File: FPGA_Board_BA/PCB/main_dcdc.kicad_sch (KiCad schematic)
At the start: 29 parts, among them Q2 IPT017N12NM6, Q3 IPT017N12NM6, Q4 IPT017N12NM6, Q5 IPT017N12NM6, U7 LM5143

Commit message: 22.11
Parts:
- renumbered D1 to D5, D2 to D6, D3 to D7, Q2 to Q1, Q3 to Q2, Q4 to Q3, Q5 to Q4, R8 to R1, R9 to R2, R10 to R3, R11 to R4, R12 to R5, R13 to R6, R14 to R7, U7 to U3
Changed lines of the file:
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@@
 		(on_board yes)
 		(dnp no)
-		(property "Reference" "#PWR022"
+		(property "Reference" "#PWR027"
 			(at 121.92 153.67 0)
 			(effects
@@
 			(project "FPGA_Board_BA"
 				(path "/fd7503bc-e7fc-4766-b224-3d1c3d7de5ff/c363a192-a091-4a49-a77c-8a6e46625814"
-					(reference "#PWR022")
+					(reference "#PWR027")
 					(unit 1)
 				)
@@
 		(on_board yes)
 		(dnp no)
-		(property "Reference" "#PWR023"
+		(property "Reference" "#PWR028"
 			(at 146.05 158.75 0)
 			(effects
@@
 			(project "FPGA_Board_BA"
 				(path "/fd7503bc-e7fc-4766-b224-3d1c3d7de5ff/c363a192-a091-4a49-a77c-8a6e46625814"
-					(reference "#PWR023")
+					(reference "#PWR028")
 					(unit 1)
 				)
@@
 		(dnp no)
 		(fields_autoplaced yes)
-		(property "Reference" "R10"
+		(property "Reference" "R3"
 			(at 101.6 52.07 90)
 			(effects
@@
 			(project ""
 				(path "/fd7503bc-e7fc-4766-b224-3d1c3d7de5ff/c363a192-a091-4a49-a77c-8a6e46625814"
-					(reference "R10")
+					(reference "R3")
 					(unit 1)
 				)
@@
 		(dnp no)
 		(fields_autoplaced yes)
-		(property "Reference" "D1"
+		(property "Reference" "D5"
 			(at 119.38 40.9574 90)
 			(effects
@@
 			(project ""
 				(path "/fd7503bc-e7fc-4766-b224-3d1c3d7de5ff/c363a192-a091-4a49-a77c-8a6e46625814"
-					(reference "D1")
+					(reference "D5")
 					(unit 1)
 				)
@@
 		(on_board yes)
 		(dnp no)
-		(property "Reference" "#PWR017"
+		(property "Reference" "#PWR022"
 			(at 62.23 44.45 0)
 			(effects
@@
 			(project "FPGA_Board_BA"
 				(path "/fd7503bc-e7fc-4766-b224-3d1c3d7de5ff/c363a192-a091-4a49-a77c-8a6e46625814"
-					(reference "#PWR017")
+					(reference "#PWR022")
 					(unit 1)
 				)
@@
 		(dnp no)
 		(fields_autoplaced yes)
-		(property "Reference" "D2"
+		(property "Reference" "D6"
 			(at 177.8 44.7674 90)
 			(effects
@@
 			(project ""
 				(path "/fd7503bc-e7fc-4766-b224-3d1c3d7de5ff/c363a192-a091-4a49-a77c-8a6e46625814"
-					(reference "D2")
+					(reference "D6")
 					(unit 1)
 				)
@@
 		(dnp no)
 		(fields_autoplaced yes)
-		(property "Reference" "R14"
+		(property "Reference" "R7"
 			(at 262.89 113.0299 0)
 			(effects
@@
 			(project ""
 				(path "/fd7503bc-e7fc-4766-b224-3d1c3d7de5ff/c363a192-a091-4a49-a77c-8a6e46625814"
-					(reference "R14")
+					(reference "R7")
 					(unit 1)
 				)
@@
 		(on_board yes)
 		(dnp no)
-		(property "Reference" "#PWR025"
+		(property "Reference" "#PWR030"
 			(at 163.83 55.88 0)
 			(effects
@@
 			(project "FPGA_Board_BA"
 				(path "/fd7503bc-e7fc-4766-b224-3d1c3d7de5ff/c363a192-a091-4a49-a77c-8a6e46625814"
-					(reference "#PWR025")
+					(reference "#PWR030")
 					(unit 1)
 				)
@@
 		(dnp no)
 		(fields_autoplaced yes)
-		(property "Reference" "Q5"
+		(property "Reference" "Q4"
 			(at 227.33 87.6299 0)
 			(effects
@@
 			(project "FPGA_Board_BA"
 				(path "/fd7503bc-e7fc-4766-b224-3d1c3d7de5ff/c363a192-a091-4a49-a77c-8a6e46625814"
-					(reference "Q5")
+					(reference "Q4")
 					(unit 1)
 				)
@@
 		(dnp no)
 		(fields_autoplaced yes)
-		(property "Reference" "R13"
+		(property "Reference" "R6"
 			(at 251.46 68.58 90)
 			(effects
@@
 			(project "FPGA_Board_BA"
 				(path "/fd7503bc-e7fc-4766-b224-3d1c3d7de5ff/c363a192-a091-4a49-a77c-8a6e46625814"
-					(reference "R13")
+					(reference "R6")
 					(unit 1)
 				)
@@
 		(dnp no)
 		(fields_autoplaced yes)
-		(property "Reference" "D3"
+		(property "Reference" "D7"
 			(at 264.16 126.0474 90)
 			(effects
@@
 			(project ""
 				(path "/fd7503bc-e7fc-4766-b224-3d1c3d7de5ff/c363a192-a091-4a49-a77c-8a6e46625814"
-					(reference "D3")
+					(reference "D7")
 					(unit 1)
 				)
@@
 		(on_board yes)
 		(dnp no)
-		(property "Reference" "Q2"
+		(property "Reference" "Q1"
 			(at 76.2 57.1499 0)
 			(effects
@@
 			(project ""
 				(path "/fd7503bc-e7fc-4766-b224-3d1c3d7de5ff/c363a192-a091-4a49-a77c-8a6e46625814"
-					(reference "Q2")
+					(reference "Q1")
 					(unit 1)
 				)
@@
 		(on_board yes)
 		(dnp no)
-		(property "Reference" "#PWR027"
+		(property "Reference" "#PWR032"
 			(at 223.52 104.14 0)
 			(effects
@@
 			(project "FPGA_Board_BA"
 				(path "/fd7503bc-e7fc-4766-b224-3d1c3d7de5ff/c363a192-a091-4a49-a77c-8a6e46625814"
-					(reference "#PWR027")
+					(reference "#PWR032")
 					(unit 1)
 				)
@@
 		(dnp no)
 		(fields_autoplaced yes)
-		(property "Reference" "R11"
+		(property "Reference" "R4"
 			(at 113.03 92.71 90)
 			(effects
@@
 			(project ""
 				(path "/fd7503bc-e7fc-4766-b224-3d1c3d7de5ff/c363a192-a091-4a49-a77c-8a6e46625814"
-					(reference "R11")
+					(reference "R4")
 					(unit 1)
 				)
@@
 		(dnp no)
 		(fields_autoplaced yes)
-		(property "Reference" "R12"
+		(property "Reference" "R5"
 			(at 201.93 55.88 90)
 			(effects
@@
 			(project "FPGA_Board_BA"
 				(path "/fd7503bc-e7fc-4766-b224-3d1c3d7de5ff/c363a192-a091-4a49-a77c-8a6e46625814"
-					(reference "R12")
+					(reference "R5")
 					(unit 1)
 				)
@@
 		(on_board yes)
 		(dnp no)
-		(property "Reference" "#PWR020"
+		(property "Reference" "#PWR025"
 			(at 99.06 139.7 0)
 			(effects
@@
 			(project "FPGA_Board_BA"
 				(path "/fd7503bc-e7fc-4766-b224-3d1c3d7de5ff/c363a192-a091-4a49-a77c-8a6e46625814"
-					(reference "#PWR020")
+					(reference "#PWR025")
 					(unit 1)
 				)
@@
 		(dnp no)
 		(fields_autoplaced yes)
-		(property "Reference" "Q4"
+		(property "Reference" "Q3"
 			(at 227.33 60.9599 0)
 			(effects
@@
 			(project "FPGA_Board_BA"
 				(path "/fd7503bc-e7fc-4766-b224-3d1c3d7de5ff/c363a192-a091-4a49-a77c-8a6e46625814"
-					(reference "Q4")
+					(reference "Q3")
 					(unit 1)
 				)
@@
 		(dnp no)
 		(fields_autoplaced yes)
-		(property "Reference" "#PWR029"
+		(property "Reference" "#PWR034"
 			(at 260.35 67.31 0)
 			(effects
@@
 			(project ""
 				(path "/fd7503bc-e7fc-4766-b224-3d1c3d7de5ff/c363a192-a091-4a49-a77c-8a6e46625814"
-					(reference "#PWR029")
+					(reference "#PWR034")
 					(unit 1)
 				)
@@
 		(on_board yes)
 		(dnp no)
-		(property "Reference" "R9"
+		(property "Reference" "R2"
 			(at 89.916 114.808 90)
 			(effects
@@
 			(project ""
 				(path "/fd7503bc-e7fc-4766-b224-3d1c3d7de5ff/c363a192-a091-4a49-a77c-8a6e46625814"
-					(reference "R9")
+					(reference "R2")
 					(unit 1)
 				)
@@
 		(on_board yes)
 		(dnp no)
-		(property "Reference" "#PWR019"
+		(property "Reference" "#PWR024"
 			(at 80.01 104.14 0)
 			(effects
@@
 			(project ""
 				(path "/fd7503bc-e7fc-4766-b224-3d1c3d7de5ff/c363a192-a091-4a49-a77c-8a6e46625814"
-					(reference "#PWR019")
+					(reference "#PWR024")
 					(unit 1)
 				)
@@
 		(dnp no)
 		(fields_autoplaced yes)
-		(property "Reference" "R8"
+		(property "Reference" "R1"
 			(at 43.18 64.77 90)
 			(effects
@@
 			(project ""
 				(path "/fd7503bc-e7fc-4766-b224-3d1c3d7de5ff/c363a192-a091-4a49-a77c-8a6e46625814"
-					(reference "R8")
+					(reference "R1")
 					(unit 1)
 				)
@@
 		(on_board yes)
 		(dnp no)
-		(property "Reference" "#PWR018"
+		(property "Reference" "#PWR023"
 			(at 76.2 139.7 0)
 			(effects
@@
 			(project "FPGA_Board_BA"
 				(path "/fd7503bc-e7fc-4766-b224-3d1c3d7de5ff/c363a192-a091-4a49-a77c-8a6e46625814"
-					(reference "#PWR018")
+					(reference "#PWR023")
 					(unit 1)
 				)
@@
 		(dnp no)
 		(fields_autoplaced yes)
-		(property "Reference" "U7"
+		(property "Reference" "U3"
 			(at 157.0833 66.04 0)
 			(effects
@@
 			(project ""
 				(path "/fd7503bc-e7fc-4766-b224-3d1c3d7de5ff/c363a192-a091-4a49-a77c-8a6e46625814"
-					(reference "U7")
+					(reference "U3")
 					(unit 1)
 				)
@@
 		(dnp no)
 		(fields_autoplaced yes)
-		(property "Reference" "Q3"
+		(property "Reference" "Q2"
 			(at 76.2 87.6299 0)
 			(effects
@@
 			(project "FPGA_Board_BA"
 				(path "/fd7503bc-e7fc-4766-b224-3d1c3d7de5ff/c363a192-a091-4a49-a77c-8a6e46625814"
-					(reference "Q3")
+					(reference "Q2")
 					(unit 1)
 				)
@@
 		(on_board yes)
 		(dnp no)
-		(property "Reference" "#PWR030"
+		(property "Reference" "#PWR035"
 			(at 260.35 138.43 0)
 			(effects
@@
 			(project "FPGA_Board_BA"
 				(path "/fd7503bc-e7fc-4766-b224-3d1c3d7de5ff/c363a192-a091-4a49-a77c-8a6e46625814"
-					(reference "#PWR030")
+					(reference "#PWR035")
 					(unit 1)
 				)
@@
 		(on_board yes)
 		(dnp no)
-		(property "Reference" "#PWR021"
+		(property "Reference" "#PWR026"
 			(at 101.6 49.53 0)
 			(effects
@@
 			(project "FPGA_Board_BA"
 				(path "/fd7503bc-e7fc-4766-b224-3d1c3d7de5ff/c363a192-a091-4a49-a77c-8a6e46625814"
-					(reference "#PWR021")
+					(reference "#PWR026")
 					(unit 1)
 				)
@@
 		(on_board yes)
 		(dnp no)
-		(property "Reference" "#PWR016"
+		(property "Reference" "#PWR021"
 			(at 38.1 43.18 0)
 			(effects
@@
 			(project "FPGA_Board_BA"
 				(path "/fd7503bc-e7fc-4766-b224-3d1c3d7de5ff/c363a192-a091-4a49-a77c-8a6e46625814"
-					(reference "#PWR016")
+					(reference "#PWR021")
 					(unit 1)
 				)
@@
 		(on_board yes)
 		(dnp no)
-		(property "Reference" "#PWR026"
+		(property "Reference" "#PWR031"
 			(at 204.47 49.53 0)
 			(effects
@@
 			(project "FPGA_Board_BA"
 				(path "/fd7503bc-e7fc-4766-b224-3d1c3d7de5ff/c363a192-a091-4a49-a77c-8a6e46625814"
-					(reference "#PWR026")
+					(reference "#PWR031")
 					(unit 1)
 				)
@@
 		(on_board yes)
 		(dnp no)
-		(property "Reference" "#PWR028"
+		(property "Reference" "#PWR033"
 			(at 238.76 41.91 0)
 			(effects
@@
 			(project "FPGA_Board_BA"
 				(path "/fd7503bc-e7fc-4766-b224-3d1c3d7de5ff/c363a192-a091-4a49-a77c-8a6e46625814"
-					(reference "#PWR028")
+					(reference "#PWR033")
 					(unit 1)
 				)
@@
 		(on_board yes)
 		(dnp no)
-		(property "Reference" "#PWR024"
+		(property "Reference" "#PWR029"
 			(at 156.21 158.75 0)
 			(effects
@@
 			(project "FPGA_Board_BA"
 				(path "/fd7503bc-e7fc-4766-b224-3d1c3d7de5ff/c363a192-a091-4a49-a77c-8a6e46625814"
-					(reference "#PWR024")
+					(reference "#PWR029")
 					(unit 1)
 				)

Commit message: exported stuff
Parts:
- D7: footprint WLIB_DO:LED_0603_1608Metric -> LED_SMD:LED_0603_1608Metric
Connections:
- net GND: now also U3.14 (PGND2), U3.17 (PGND1), U3.35 (AGND)
- net at C25.1, D6.1 (K): now also U3.11 (HB2)

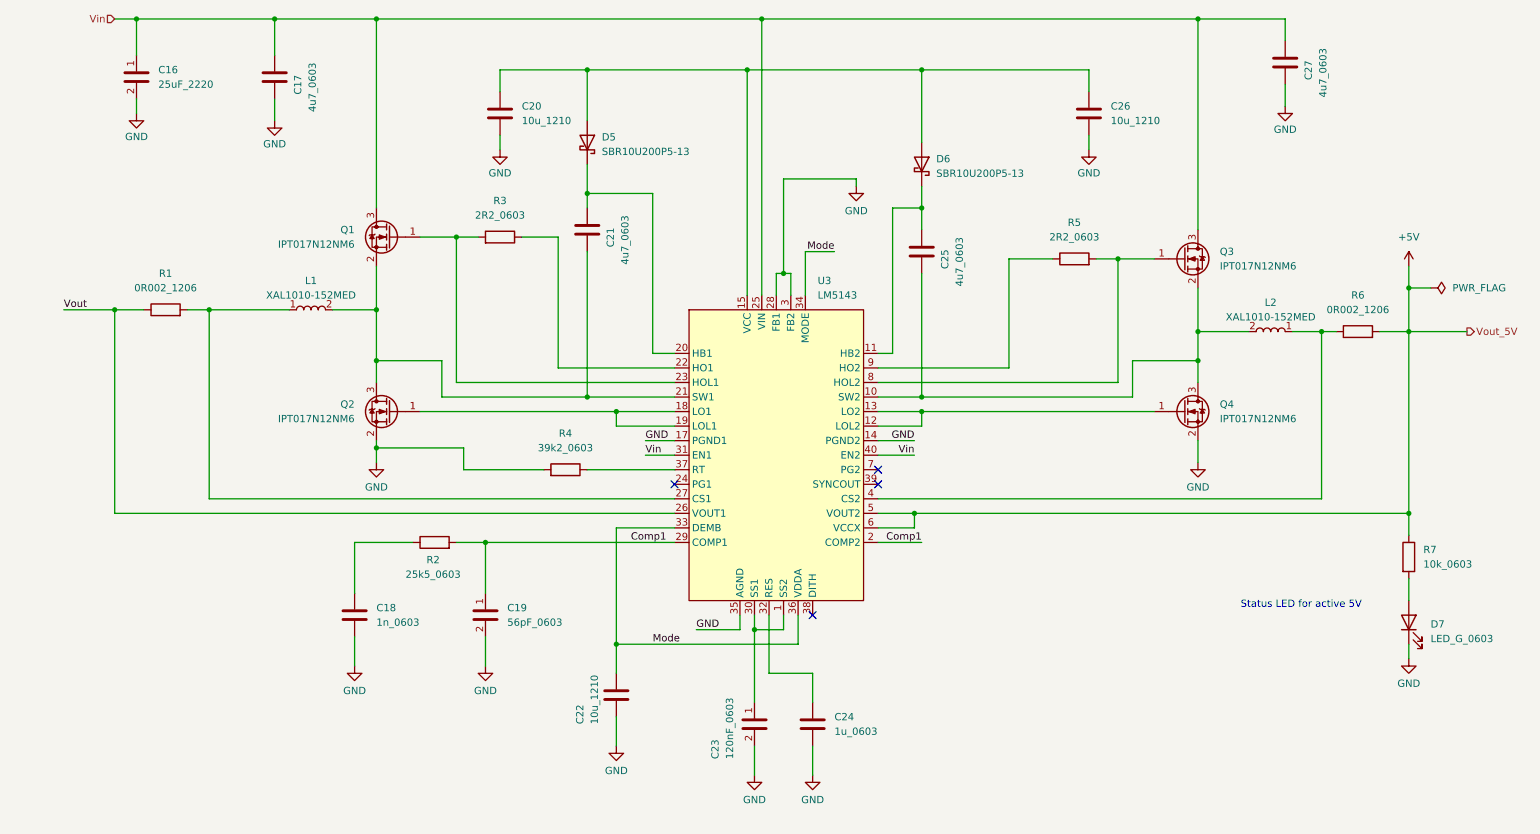
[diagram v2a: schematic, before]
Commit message: placement of Power DCDC and Buffers ready
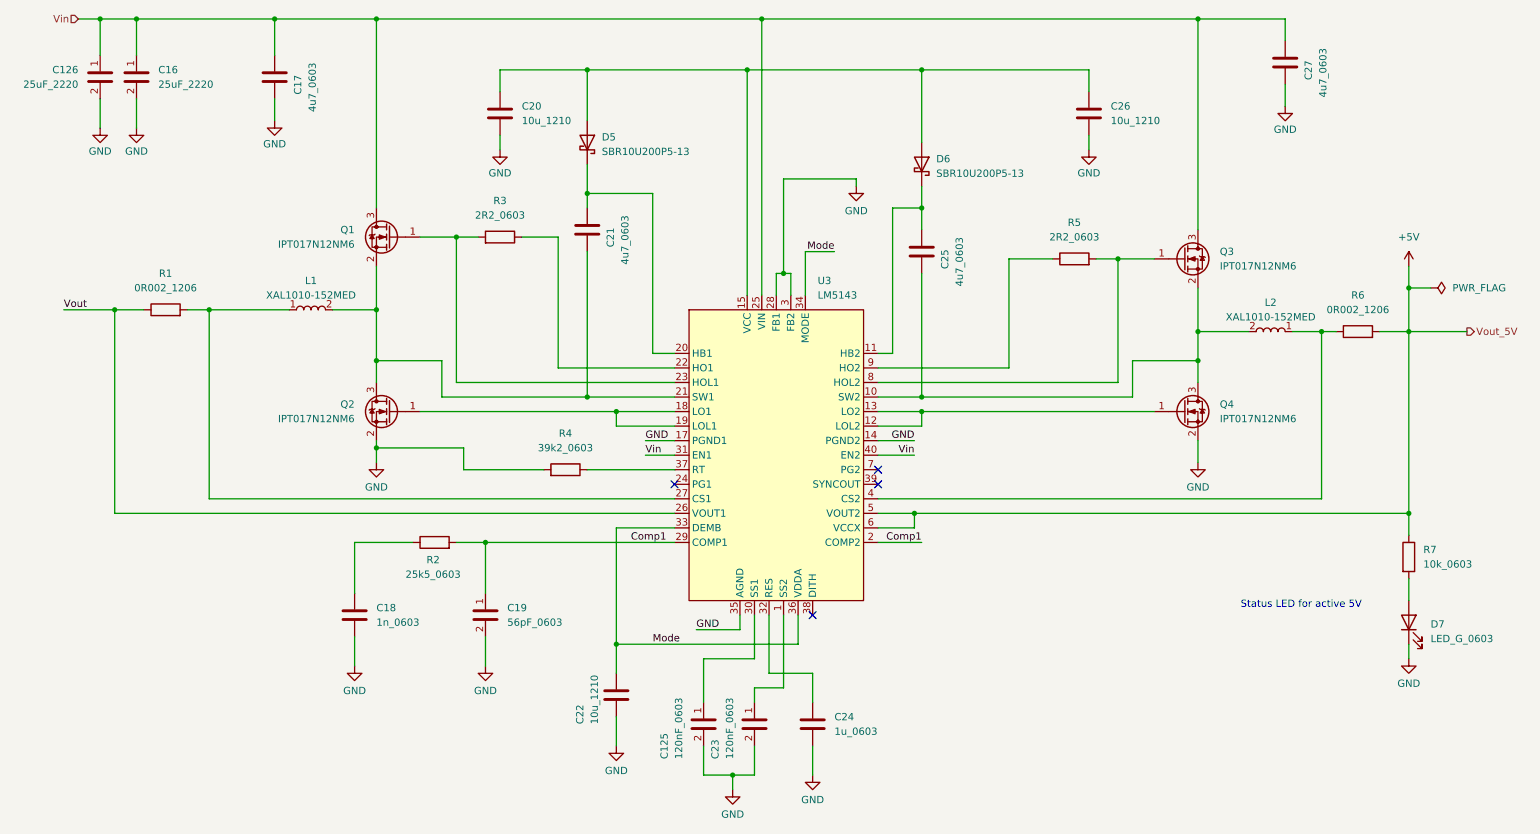
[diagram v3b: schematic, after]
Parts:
- added C125: 120nF_0603, Capacitor_SMD:C_0603_1608Metric_Pad1.08x0.95mm_HandSolder, symbol MYLIB_Misc:120nF_0603
- added C126: 25uF_2220, Capacitor_SMD:C_2220_5650Metric_Pad1.97x5.40mm_HandSolder, symbol MYLIB_Misc:15uF_2220
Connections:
- net GND: now also C125.2, C126.2
- net Vin: now also C126.1
- net at C23.1, U3.1 (SS2): no longer U3.30 (SS1)
- new net: C125.1, U3.30 (SS1)

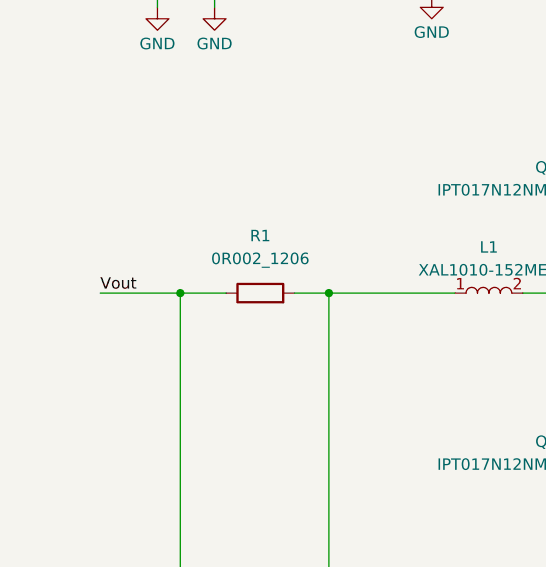
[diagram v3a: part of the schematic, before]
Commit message: layout of islands is ready
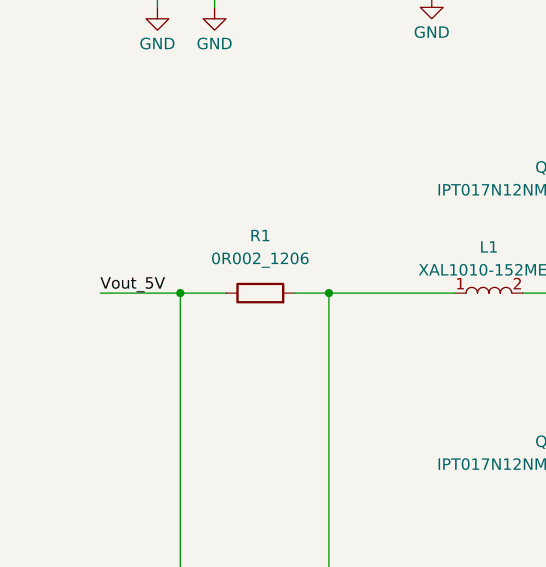
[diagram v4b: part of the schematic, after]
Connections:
- net Vout is gone; now on net +5V: R1.1, U3.26 (VOUT1)
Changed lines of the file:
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@@
 		)
 	)
-	(label "Vout"
+	(label "Vout_5V"
 		(at 25.4 71.12 0)
 		(effects

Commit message: Placement optimised
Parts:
- removed L1, L2: XAL1010-152MED, Inductor_SMD:L_Coilcraft_XAL1010-XXX, symbol MYLIB_Misc:XAL1010-152MED
- removed Q1, Q2, Q3, Q4: IPT017N12NM6, Package_TO_SOT_SMD:Infineon_PG-HSOF-8-1, symbol MYLIB_Misc:IPT017N12NM6
- removed R1, R6: 0R002_1206, Resistor_SMD:R_1206_3216Metric_Pad1.30x1.75mm_HandSolder, symbol MYLIB_Misc:0R002_1206
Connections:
- net Leg-2/R_I+: now reaches U3.4 (CS2)
- net Leg-2/SW: now reaches C25.2, U3.10 (SW2)
- net Leg-1/Gate_H: now reaches R3.1, U3.23 (HOL1)
- net Leg-2/Gate_L: now reaches U3.12 (LOL2), U3.13 (LO2)
- net Leg-1/SW: now reaches C21.2, U3.21 (SW1)
- net Leg-1/R_I+: now reaches U3.27 (CS1)
- net Leg-2/Gate_H: now reaches R5.1, U3.8 (HOL2)
- net Leg-1/Gate_L: now reaches U3.18 (LO1), U3.19 (LOL1)
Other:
- added sheet Leg-1 (leg_1.kicad_sch)
- added sheet Leg-2 (leg_1.kicad_sch)
- moved on the sheet: R4

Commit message: PCB left side almost finished + some optimization in schematics
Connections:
- net GND: now also U3.41 (Pad)
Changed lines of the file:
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@@
 	(wire
 		(pts
+			(xy 158.75 124.46) (xy 158.75 127)
+		)
+		(stroke
+			(width 0)
+			(type default)
+		)
+	)
+	(wire
+		(pts
 			(xy 151.13 64.77) (xy 152.4 64.77)
 		)
@@
 		(pin "17"
 		)
+		(pin "41"
+		)
 		(instances
 			(project ""
@@
 					(unit 1)
 				)
+			)
+		)
+	)
+	(symbol
+		(lib_id "power:GND")
+		(at 158.75 127 0)
+		(unit 1)
+		(exclude_from_sim no)
+		(in_bom yes)
+		(on_board yes)
+		(dnp no)
+		(property "Reference" "#PWR044"
+			(at 158.75 133.35 0)
+			(effects
+				(font
+					(size 1.27 1.27)
+				)
+				(hide yes)
+			)
+		)
+		(property "Value" "GND"
+			(at 158.75 131.318 0)
+			(effects
+				(font
+					(size 1.27 1.27)
+				)
+			)
+		)
+		(property "Footprint" ""
+			(at 158.75 127 0)
+			(effects
+				(font
+					(size 1.27 1.27)
+				)
+				(hide yes)
+			)
+		)
+		(property "Datasheet" ""
+			(at 158.75 127 0)
+			(effects
+				(font
+					(size 1.27 1.27)
+				)
+				(hide yes)
+			)
+		)
+		(property "Description" "Power symbol creates a global label with name \"GND\" , ground"
+			(at 158.75 127 0)
+			(effects
+				(font
+					(size 1.27 1.27)
+				)
+				(hide yes)
+			)
+		)
+		(pin "1"
+		)
+		(instances
+			(project "FPGA_Board_BA"
+				(path "/fd7503bc-e7fc-4766-b224-3d1c3d7de5ff/c363a192-a091-4a49-a77c-8a6e46625814"
+					(reference "#PWR044")
+					(unit 1)
+				)

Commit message: PCB ready to be ordered
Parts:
- added C177, C178: 25uF_2220, Capacitor_SMD:C_2220_5650Metric_Pad1.97x5.40mm_HandSolder, symbol MYLIB_Misc:15uF_2220
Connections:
- net GND: now also C177.2, C178.2
- net Vin: now also C177.1, C178.1
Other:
- moved on the sheet: C16, C17
